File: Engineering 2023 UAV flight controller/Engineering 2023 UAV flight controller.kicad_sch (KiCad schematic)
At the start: 82 parts, among them J1 Micro_SD_Card, J2 ESC speed control, J3 USB_C_Receptacle_USB2.0, J4 Conn_Coaxial, J5 external power rail, J6 Board GPIO and the Lora DIO, J7 external ground rail, M1 Aileron Left, M2 Aileron Right, M3 Elevator Left, M4 Elevator Right, SW1 SW_SPDT, SW2 4FSH922, SW3 SW_Push, U1 W25Q128JVS, U2 NCP1117-3.3_TO252, U3 LM350_TO220, U4 RP2040, U5 LPS25HB, U6 MPU-6050, U7 MMC5983MA, U8 E28-2G4M27S, U9 NEO-M8N, Y1 ABLS-12.000MHZ-B4-T

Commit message: started component placement, finished placeing power?
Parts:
- added R18, R19: 2k7, Resistor_SMD:R_0603_1608Metric, symbol Device:R
- R2: footprint Resistor_SMD:R_0603_1608Metric -> Potentiometer_SMD:Potentiometer_Bourns_3314R-GM5_Vertical
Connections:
- net 3.3v rail: now also R18.1, R19.1
- net IMU_SCL: now also R18.2
- net IMU_SDA: now also R19.2
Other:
- note added: "dont have to fill these"
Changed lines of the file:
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@@
   (junction (at 369.57 208.28) (diameter 0) (color 0 0 0 0)
   )
+  (junction (at 231.14 60.96) (diameter 0) (color 0 0 0 0)
+  )
   (junction (at 204.47 71.12) (diameter 0) (color 0 0 0 0)
   )
@@
   (junction (at 379.73 105.41) (diameter 0) (color 0 0 0 0)
   )
+  (junction (at 237.49 60.96) (diameter 0) (color 0 0 0 0)
+  )
   (junction (at 232.41 110.49) (diameter 0) (color 0 0 0 0)
   )
@@
     (stroke (width 0) (type default) (color 0 0 0 0))
   )
-  (wire (pts (xy 198.12 36.83) (xy 215.9 36.83))
+  (wire (pts (xy 198.12 36.83) (xy 237.49 36.83))
     (stroke (width 0) (type default) (color 0 0 0 0))
   )
@@
     (stroke (width 0) (type default) (color 0 0 0 0))
   )
+  (wire (pts (xy 231.14 60.96) (xy 227.33 60.96))
+    (stroke (width 0) (type default) (color 0 0 0 0))
+  )
   (wire (pts (xy 146.05 229.87) (xy 171.45 229.87))
     (stroke (width 0) (type default) (color 0 0 0 0))
@@
     (stroke (width 0) (type default) (color 0 0 0 0))
   )
+  (wire (pts (xy 231.14 41.91) (xy 231.14 46.99))
+    (stroke (width 0) (type default) (color 0 0 0 0))
+  )
   (wire (pts (xy 83.82 245.11) (xy 95.25 245.11))
     (stroke (width 0) (type default) (color 0 0 0 0))
@@
     (stroke (width 0) (type default) (color 0 0 0 0))
   )
-  (wire (pts (xy 264.16 60.96) (xy 227.33 60.96))
+  (wire (pts (xy 237.49 54.61) (xy 237.49 60.96))
+    (stroke (width 0) (type default) (color 0 0 0 0))
+  )
+  (wire (pts (xy 264.16 60.96) (xy 237.49 60.96))
     (stroke (width 0) (type default) (color 0 0 0 0))
   )
@@
     (stroke (width 0) (type default) (color 0 0 0 0))
   )
+  (wire (pts (xy 231.14 54.61) (xy 231.14 60.96))
+    (stroke (width 0) (type default) (color 0 0 0 0))
+  )
   (wire (pts (xy 356.87 21.59) (xy 356.87 22.86))
     (stroke (width 0) (type default) (color 0 0 0 0))
@@
     (stroke (width 0) (type default) (color 0 0 0 0))
   )
+  (wire (pts (xy 237.49 60.96) (xy 231.14 60.96))
+    (stroke (width 0) (type default) (color 0 0 0 0))
+  )
   (wire (pts (xy 113.03 147.32) (xy 104.14 147.32))
     (stroke (width 0) (type default) (color 0 0 0 0))
@@
     (stroke (width 0) (type default) (color 0 0 0 0))
   )
-  (wire (pts (xy 198.12 41.91) (xy 215.9 41.91))
+  (wire (pts (xy 198.12 41.91) (xy 231.14 41.91))
     (stroke (width 0) (type default) (color 0 0 0 0))
   )
@@
     (stroke (width 0) (type default) (color 0 0 0 0))
   )
+  (wire (pts (xy 237.49 36.83) (xy 237.49 46.99))
+    (stroke (width 0) (type default) (color 0 0 0 0))
+  )
   (wire (pts (xy 83.82 217.17) (xy 95.25 217.17))
     (stroke (width 0) (type default) (color 0 0 0 0))
@@
     (effects (font (size 1.27 1.27)) (justify left bottom))
   )
-  (text "you can add bars :>\n" (at 219.71 44.45 0)
+  (text "you can add bars :>\n" (at 208.28 46.99 0)
     (effects (font (size 1.27 1.27)) (justify left bottom))
   )
@@
     (effects (font (size 1.27 1.27)) (justify left bottom))
   )
+  (text "dont have to fill these\n" (at 238.76 46.99 0)
+    (effects (font (size 1.27 1.27)) (justify left bottom))
+  )
   (text "close together\n" (at 68.58 217.17 0)
     (effects (font (size 1.27 1.27)) (justify left bottom))
@@
       (effects (font (size 1.27 1.27)) (justify left))
     )
-    (property "Footprint" "Resistor_SMD:R_0603_1608Metric" (id 2) (at 116.332 46.99 90)
+    (property "Footprint" "Potentiometer_SMD:Potentiometer_Bourns_3314R-GM5_Vertical" (id 2) (at 116.332 46.99 90)
       (effects (font (size 1.27 1.27)) hide)
     )
@@
     (pin "1")
   )
+  (symbol (lib_id "Device:R") (at 231.14 50.8 180) (unit 1)
+    (in_bom yes) (on_board yes)
+    (property "Reference" "R18" (id 0) (at 228.6 50.8 0))
+    (property "Value" "2k7" (id 1) (at 228.6 54.61 0))
+    (property "Footprint" "Resistor_SMD:R_0603_1608Metric" (id 2) (at 232.918 50.8 90)
+      (effects (font (size 1.27 1.27)) hide)
+    )
+    (property "Datasheet" "~" (id 3) (at 231.14 50.8 0)
+      (effects (font (size 1.27 1.27)) hide)
+    )
+    (pin "1")
+    (pin "2")
+  )
   (symbol (lib_id "Device:R") (at 370.84 99.06 90) (unit 1)
     (in_bom yes) (on_board yes)
@@
     (pin "3")
   )
+  (symbol (lib_id "Device:R") (at 237.49 50.8 180) (unit 1)
+    (in_bom yes) (on_board yes)
+    (property "Reference" "R19" (id 0) (at 234.95 50.8 0))
+    (property "Value" "2k7" (id 1) (at 234.95 54.61 0))
+    (property "Footprint" "Resistor_SMD:R_0603_1608Metric" (id 2) (at 239.268 50.8 90)
+      (effects (font (size 1.27 1.27)) hide)
+    )
+    (property "Datasheet" "~" (id 3) (at 237.49 50.8 0)
+      (effects (font (size 1.27 1.27)) hide)
+    )
+    (pin "1")
+    (pin "2")
+  )
   (symbol (lib_id "Device:C") (at 135.89 167.64 0) (unit 1)
     (in_bom yes) (on_board yes) (fields_autoplaced)
@@
     )
     (path "/3a54be61-d587-43af-a41b-390d94c7c9c1"
-      (reference "R2") (unit 1) (value "R_Trim") (footprint "Resistor_SMD:R_0603_1608Metric")
+      (reference "R2") (unit 1) (value "R_Trim") (footprint "Potentiometer_SMD:Potentiometer_Bourns_3314R-GM5_Vertical")
     )
     (path "/190db31f-23de-4a5f-b028-8237ba532468"
@@
       (reference "R17") (unit 1) (value "10") (footprint "Resistor_SMD:R_0603_1608Metric")
     )
+    (path "/883a228f-7cdc-4669-8a94-309e1bfae9f1"
+      (reference "R18") (unit 1) (value "2k7") (footprint "Resistor_SMD:R_0603_1608Metric")
+    )
+    (path "/a859c833-32d1-48a4-9b68-1dc6f9544e3b"
+      (reference "R19") (unit 1) (value "2k7") (footprint "Resistor_SMD:R_0603_1608Metric")
+    )
     (path "/4c82a77c-290f-4e00-8453-9b533ca74c97"

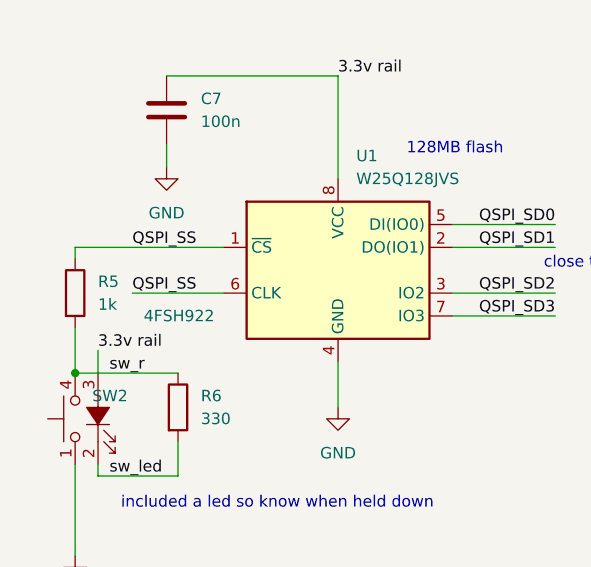
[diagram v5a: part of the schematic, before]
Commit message: some more component placement
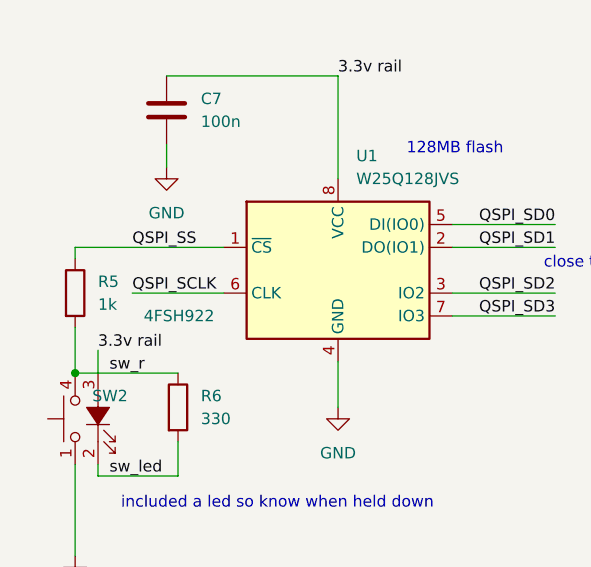
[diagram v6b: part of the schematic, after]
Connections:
- net QSPI_SCLK: now also U1.6 (CLK)
- net QSPI_SS: no longer U1.6 (CLK)
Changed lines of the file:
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@@
     (effects (font (size 1.27 1.27)) (justify left bottom))
   )
-  (label "QSPI_SS" (at 22.86 219.71 0)
+  (label "QSPI_SCLK" (at 22.86 219.71 0)
     (effects (font (size 1.27 1.27)) (justify left bottom))
   )

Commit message: finished first layout itteration
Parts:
- added C36: 1u, Capacitor_SMD:C_0603_1608Metric, symbol Device:C
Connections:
- net 3.3v rail: now also C36.2
- net GND: now also C36.1
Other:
- note added: "dnf"
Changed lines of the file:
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@@
   (junction (at 118.11 40.64) (diameter 0) (color 0 0 0 0)
   )
+  (junction (at 331.47 78.74) (diameter 0) (color 0 0 0 0)
+  )
   (junction (at 43.18 269.24) (diameter 0) (color 0 0 0 0)
   )
@@
   (junction (at 283.21 36.83) (diameter 0) (color 0 0 0 0)
   )
+  (junction (at 331.47 86.36) (diameter 0) (color 0 0 0 0)
+  )
   (no_connect (at 247.65 255.27))
   (no_connect (at 379.73 119.38))
@@
     (stroke (width 0) (type default) (color 0 0 0 0))
   )
+  (wire (pts (xy 331.47 78.74) (xy 342.9 78.74))
+    (stroke (width 0) (type default) (color 0 0 0 0))
+  )
   (wire (pts (xy 261.62 73.66) (xy 264.16 73.66))
     (stroke (width 0) (type default) (color 0 0 0 0))
@@
     (stroke (width 0) (type default) (color 0 0 0 0))
   )
+  (wire (pts (xy 331.47 86.36) (xy 342.9 86.36))
+    (stroke (width 0) (type default) (color 0 0 0 0))
+  )
   (wire (pts (xy 368.3 73.66) (xy 388.62 73.66))
     (stroke (width 0) (type default) (color 0 0 0 0))
@@
     (effects (font (size 1.27 1.27)) (justify left bottom))
   )
+  (text "dnf" (at 180.34 69.85 0)
+    (effects (font (size 1.27 1.27)) (justify left bottom))
+  )
   (text "also 12, 13, 24\n" (at 264.16 269.24 180)
     (effects (font (size 1.27 1.27)) (justify right bottom))
@@
     (pin "1")
   )
+  (symbol (lib_id "Device:C") (at 342.9 82.55 180) (unit 1)
+    (in_bom yes) (on_board yes) (fields_autoplaced)
+    (property "Reference" "C36" (id 0) (at 346.71 81.2799 0)
+      (effects (font (size 1.27 1.27)) (justify right))
+    )
+    (property "Value" "1u" (id 1) (at 346.71 83.8199 0)
+      (effects (font (size 1.27 1.27)) (justify right))
+    )
+    (property "Footprint" "Capacitor_SMD:C_0603_1608Metric" (id 2) (at 341.9348 78.74 0)
+      (effects (font (size 1.27 1.27)) hide)
+    )
+    (property "Datasheet" "~" (id 3) (at 342.9 82.55 0)
+      (effects (font (size 1.27 1.27)) hide)
+    )
+    (pin "1")
+    (pin "2")
+  )
   (symbol (lib_id "Device:C") (at 228.6 213.36 0) (unit 1)
     (in_bom yes) (on_board yes) (fields_autoplaced)
@@
       (reference "C35") (unit 1) (value "47p") (footprint "Capacitor_SMD:C_0603_1608Metric")
     )
+    (path "/d65343f2-c66f-4705-8ffc-5027e219d412"
+      (reference "C36") (unit 1) (value "1u") (footprint "Capacitor_SMD:C_0603_1608Metric")
+    )
     (path "/72c450af-5577-4528-bb4f-2acfd572dc3a"

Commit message: started routing
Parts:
- added C37: 100n, Capacitor_SMD:C_0603_1608Metric, symbol Device:C
- J2, M1, M2, M3, M4: footprint Connector_PinSocket_2.54mm:PinSocket_1x03_P2.54mm_Vertical -> Connector_PinHeader_2.54mm:PinHeader_1x03_P2.54mm_Vertical
- J6: footprint Connector_PinSocket_2.54mm:PinSocket_1x13_P2.54mm_Vertical -> Connector_PinHeader_2.54mm:PinHeader_1x13_P2.54mm_Vertical
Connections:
- net 3.3v rail: now also C37.1
- net GND: now also C37.2
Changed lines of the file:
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@@
   (junction (at 227.33 60.96) (diameter 0) (color 0 0 0 0)
   )
+  (junction (at 199.39 147.32) (diameter 0) (color 0 0 0 0)
+  )
   (junction (at 209.55 71.12) (diameter 0) (color 0 0 0 0)
   )
@@
     (stroke (width 0) (type default) (color 0 0 0 0))
   )
+  (wire (pts (xy 199.39 154.94) (xy 209.55 154.94))
+    (stroke (width 0) (type default) (color 0 0 0 0))
+  )
   (wire (pts (xy 83.82 234.95) (xy 95.25 234.95))
     (stroke (width 0) (type default) (color 0 0 0 0))
@@
     (stroke (width 0) (type default) (color 0 0 0 0))
   )
+  (wire (pts (xy 199.39 147.32) (xy 209.55 147.32))
+    (stroke (width 0) (type default) (color 0 0 0 0))
+  )
   (wire (pts (xy 58.42 222.25) (xy 69.85 222.25))
     (stroke (width 0) (type default) (color 0 0 0 0))
@@
       (effects (font (size 1.27 1.27)) (justify left))
     )
-    (property "Footprint" "Connector_PinSocket_2.54mm:PinSocket_1x03_P2.54mm_Vertical" (id 2) (at 396.24 50.546 0)
+    (property "Footprint" "Connector_PinHeader_2.54mm:PinHeader_1x03_P2.54mm_Vertical" (id 2) (at 396.24 50.546 0)
       (effects (font (size 1.27 1.27)) hide)
     )
@@
       (effects (font (size 1.27 1.27)) (justify left))
     )
-    (property "Footprint" "Connector_PinSocket_2.54mm:PinSocket_1x03_P2.54mm_Vertical" (id 2) (at 396.24 63.246 0)
+    (property "Footprint" "Connector_PinHeader_2.54mm:PinHeader_1x03_P2.54mm_Vertical" (id 2) (at 396.24 63.246 0)
       (effects (font (size 1.27 1.27)) hide)
     )
@@
     (pin "9")
   )
+  (symbol (lib_id "Device:C") (at 209.55 151.13 0) (unit 1)
+    (in_bom yes) (on_board yes) (fields_autoplaced)
+    (property "Reference" "C37" (id 0) (at 213.36 149.8599 0)
+      (effects (font (size 1.27 1.27)) (justify left))
+    )
+    (property "Value" "100n" (id 1) (at 213.36 152.3999 0)
+      (effects (font (size 1.27 1.27)) (justify left))
+    )
+    (property "Footprint" "Capacitor_SMD:C_0603_1608Metric" (id 2) (at 210.5152 154.94 0)
+      (effects (font (size 1.27 1.27)) hide)
+    )
+    (property "Datasheet" "~" (id 3) (at 209.55 151.13 0)
+      (effects (font (size 1.27 1.27)) hide)
+    )
+    (pin "1")
+    (pin "2")
+  )
   (symbol (lib_id "power:GND") (at 232.41 113.03 0) (unit 1)
     (in_bom yes) (on_board yes)
@@
       (effects (font (size 1.27 1.27)) (justify left))
     )
-    (property "Footprint" "Connector_PinSocket_2.54mm:PinSocket_1x03_P2.54mm_Vertical" (id 2) (at 396.24 39.116 0)
+    (property "Footprint" "Connector_PinHeader_2.54mm:PinHeader_1x03_P2.54mm_Vertical" (id 2) (at 396.24 39.116 0)
       (effects (font (size 1.27 1.27)) hide)
     )
@@
       (effects (font (size 1.27 1.27)) (justify left))
     )
-    (property "Footprint" "Connector_PinSocket_2.54mm:PinSocket_1x03_P2.54mm_Vertical" (id 2) (at 396.24 27.686 0)
+    (property "Footprint" "Connector_PinHeader_2.54mm:PinHeader_1x03_P2.54mm_Vertical" (id 2) (at 396.24 27.686 0)
       (effects (font (size 1.27 1.27)) hide)
     )
@@
       (effects (font (size 1.27 1.27)) (justify left))
     )
-    (property "Footprint" "Connector_PinSocket_2.54mm:PinSocket_1x13_P2.54mm_Vertical" (id 2) (at 384.81 161.29 0)
+    (property "Footprint" "Connector_PinHeader_2.54mm:PinHeader_1x13_P2.54mm_Vertical" (id 2) (at 384.81 161.29 0)
       (effects (font (size 1.27 1.27)) hide)
     )
@@
       (effects (font (size 1.27 1.27)) (justify left))
     )
-    (property "Footprint" "Connector_PinSocket_2.54mm:PinSocket_1x03_P2.54mm_Vertical" (id 2) (at 393.7 71.12 0)
+    (property "Footprint" "Connector_PinHeader_2.54mm:PinHeader_1x03_P2.54mm_Vertical" (id 2) (at 393.7 71.12 0)
       (effects (font (size 1.27 1.27)) hide)
     )
@@
       (reference "C36") (unit 1) (value "1u") (footprint "Capacitor_SMD:C_0603_1608Metric")
     )
+    (path "/6894e1d6-44af-4abf-899d-a1e8944eb7fa"
+      (reference "C37") (unit 1) (value "100n") (footprint "Capacitor_SMD:C_0603_1608Metric")
+    )
     (path "/72c450af-5577-4528-bb4f-2acfd572dc3a"
       (reference "D1") (unit 1) (value "LED_GREEN") (footprint "LED_SMD:LED_0603_1608Metric")
@@
     )
     (path "/ee2d7551-8ac1-4618-9348-753907aeb052"
-      (reference "J2") (unit 1) (value "ESC speed control") (footprint "Connector_PinSocket_2.54mm:PinSocket_1x03_P2.54mm_Vertical")
+      (reference "J2") (unit 1) (value "ESC speed control") (footprint "Connector_PinHeader_2.54mm:PinHeader_1x03_P2.54mm_Vertical")
     )
     (path "/4e4874c5-bb67-487a-a563-b4752538e5fc"
@@
     )
     (path "/e2b9803d-442f-4aec-a59d-59cc459a63cf"
-      (reference "J6") (unit 1) (value "Board GPIO and the Lora DIO") (footprint "Connector_PinSocket_2.54mm:PinSocket_1x13_P2.54mm_Vertical")
+      (reference "J6") (unit 1) (value "Board GPIO and the Lora DIO") (footprint "Connector_PinHeader_2.54mm:PinHeader_1x13_P2.54mm_Vertical")
     )
     (path "/9ee82663-1215-434b-ae2c-e1374e4dec94"
@@
     )
     (path "/d40a1cc5-fbc2-4c1e-9349-e721bb07408e"
-      (reference "M1") (unit 1) (value "Aileron Left") (footprint "Connector_PinSocket_2.54mm:PinSocket_1x03_P2.54mm_Vertical")
+      (reference "M1") (unit 1) (value "Aileron Left") (footprint "Connector_PinHeader_2.54mm:PinHeader_1x03_P2.54mm_Vertical")
     )
     (path "/a5803e7c-8b9f-45cb-9ce9-ade452865f1b"
-      (reference "M2") (unit 1) (value "Aileron Right") (footprint "Connector_PinSocket_2.54mm:PinSocket_1x03_P2.54mm_Vertical")
+      (reference "M2") (unit 1) (value "Aileron Right") (footprint "Connector_PinHeader_2.54mm:PinHeader_1x03_P2.54mm_Vertical")
     )
     (path "/10ec48c8-c7b5-43a4-bb63-38ddcdfa745e"
-      (reference "M3") (unit 1) (value "Elevator Left") (footprint "Connector_PinSocket_2.54mm:PinSocket_1x03_P2.54mm_Vertical")
+      (reference "M3") (unit 1) (value "Elevator Left") (footprint "Connector_PinHeader_2.54mm:PinHeader_1x03_P2.54mm_Vertical")
     )
     (path "/4e2503e3-7522-4959-b540-6c7684261f30"
-      (reference "M4") (unit 1) (value "Elevator Right") (footprint "Connector_PinSocket_2.54mm:PinSocket_1x03_P2.54mm_Vertical")
+      (reference "M4") (unit 1) (value "Elevator Right") (footprint "Connector_PinHeader_2.54mm:PinHeader_1x03_P2.54mm_Vertical")
     )
     (path "/ef66f17a-ab37-4377-b19b-d4919b418c71"
